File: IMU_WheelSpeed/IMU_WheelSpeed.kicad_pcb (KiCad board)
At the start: 2 copper layers, 10 parts, among them J1 Conn_01x06_Socket, U1 PeripheralSOM, U2 LSM6DSL, U4 TPS71518__SC70

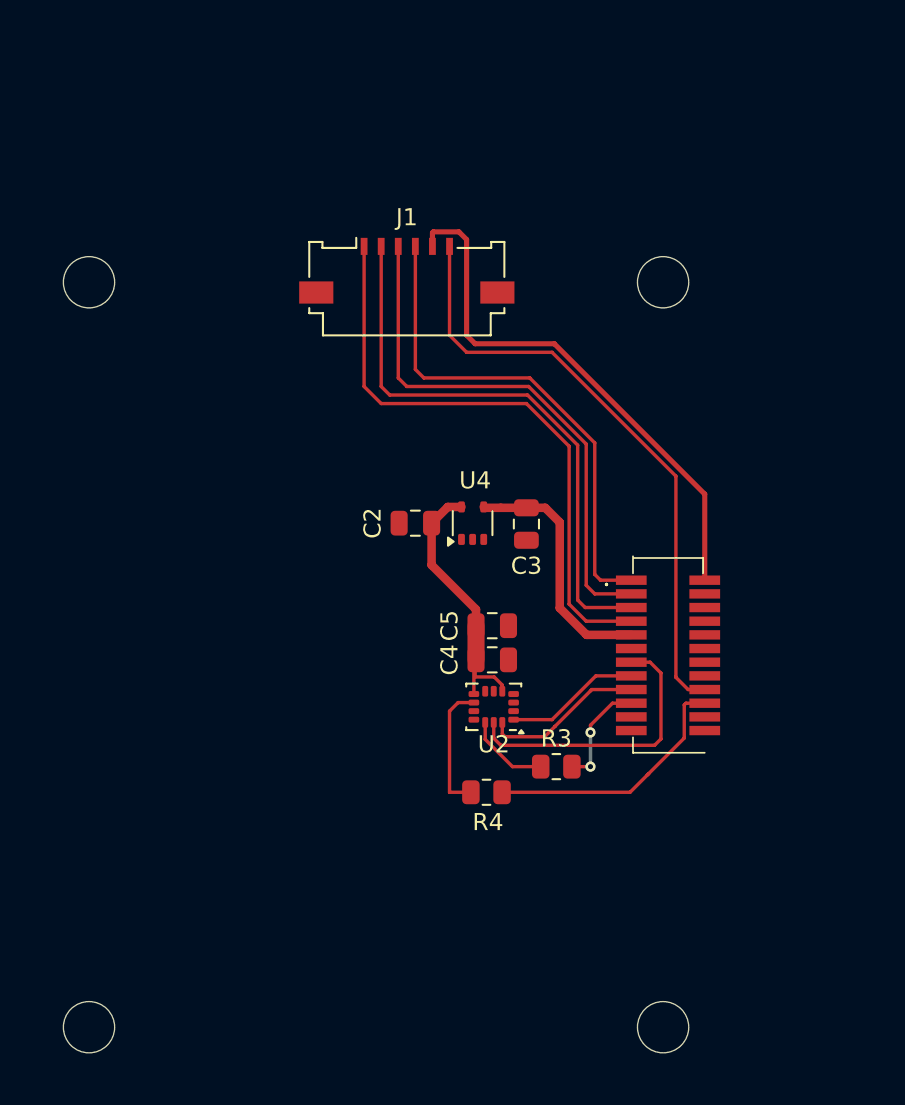
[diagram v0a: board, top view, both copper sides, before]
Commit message: added to schematic
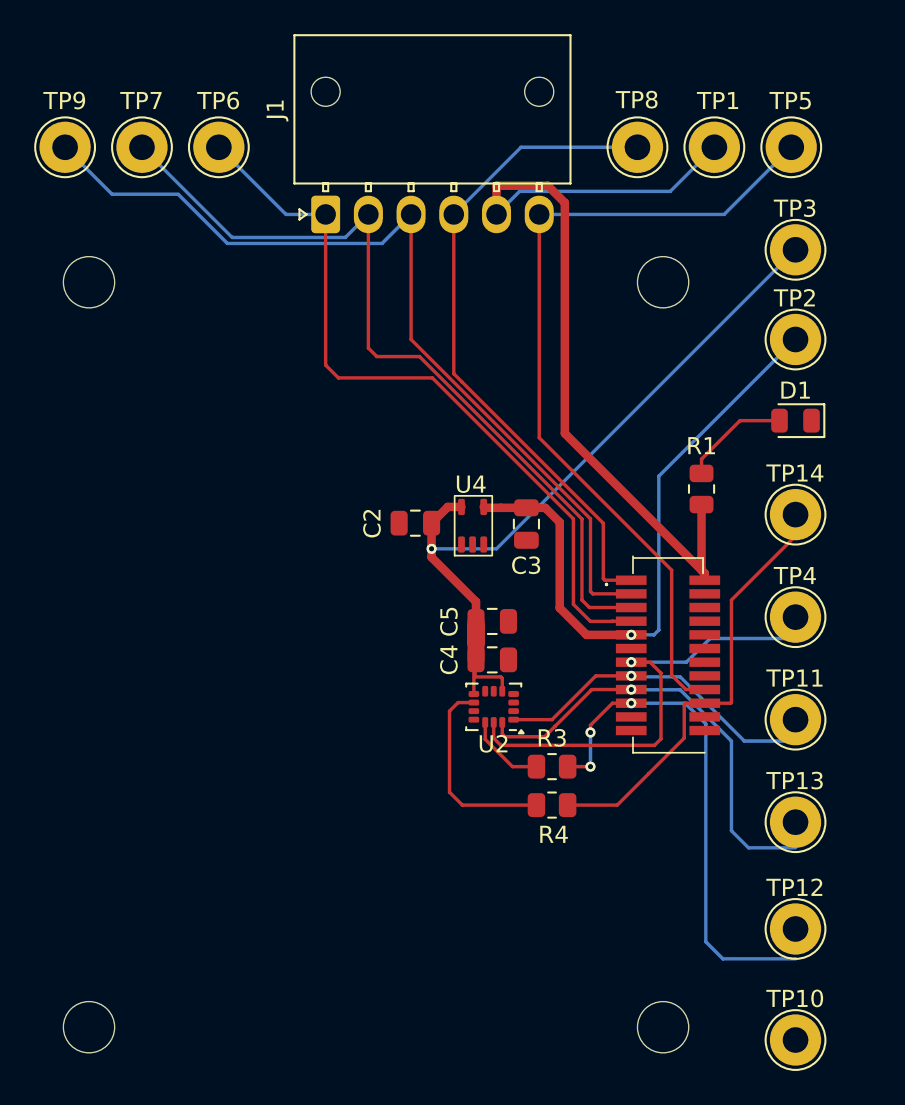
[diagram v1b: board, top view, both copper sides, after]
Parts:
- added D1: LED, LED_SMD:LED_0805_2012Metric, F.Cu at (170.8, 74.0)
- added R1: 1k, Resistor_SMD:R_0805_2012Metric, F.Cu at (165.2, 78.0)
- added TP1: VDD, TestPoint:TestPoint_THTPad_D3.0mm_Drill1.5mm, F.Cu at (166.0, 58.0)
- added TP10: VDD, TestPoint:TestPoint_THTPad_D3.0mm_Drill1.5mm, F.Cu at (170.8, 110.2)
- added TP11: VDD, TestPoint:TestPoint_THTPad_D3.0mm_Drill1.5mm, F.Cu at (170.8, 91.5)
- added TP12: VDD, TestPoint:TestPoint_THTPad_D3.0mm_Drill1.5mm, F.Cu at (170.8, 103.8)
- added TP13: VDD, TestPoint:TestPoint_THTPad_D3.0mm_Drill1.5mm, F.Cu at (170.8, 97.5)
- added TP14: VDD, TestPoint:TestPoint_THTPad_D3.0mm_Drill1.5mm, F.Cu at (170.8, 79.5)
- added TP2: VDD, TestPoint:TestPoint_THTPad_D3.0mm_Drill1.5mm, F.Cu at (170.8, 69.2)
- added TP3: VDD, TestPoint:TestPoint_THTPad_D3.0mm_Drill1.5mm, F.Cu at (170.8, 64.0)
- added TP4: VDD, TestPoint:TestPoint_THTPad_D3.0mm_Drill1.5mm, F.Cu at (170.8, 85.5)
- added TP5: VDD, TestPoint:TestPoint_THTPad_D3.0mm_Drill1.5mm, F.Cu at (170.5, 58.0)
- added TP6: VDD, TestPoint:TestPoint_THTPad_D3.0mm_Drill1.5mm, F.Cu at (137.0, 58.0)
- added TP7: VDD, TestPoint:TestPoint_THTPad_D3.0mm_Drill1.5mm, F.Cu at (132.5, 58.0)
- added TP8: VDD, TestPoint:TestPoint_THTPad_D3.0mm_Drill1.5mm, F.Cu at (161.5, 58.0)
- added TP9: VDD, TestPoint:TestPoint_THTPad_D3.0mm_Drill1.5mm, F.Cu at (128.0, 58.0)
- J1: footprint Connector_FFC-FPC:Molex_200528-0060_1x06-1MP_P1.00mm_Horizontal -> Connector_Molex:Molex_Nano-Fit_105313-xx06_1x06_P2.50mm_Horizontal
- U4: footprint Package_TO_SOT_SMD:SOT-353_SC-70-5 -> UTSVT_Special:LDO_3.3_to_1.8_2.2mmx1.3mm
- moved J1 5.50 mm to (143.2, 61.9), turned to 90 degrees
- moved U4 4.95 mm to (146.9, 80.0)
- moved R4 3.91 mm to (156.5, 96.5)
- moved C5 0.25 mm to (153.0, 85.8)
- moved R3 0.25 mm to (156.5, 94.2)
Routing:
- net <NO NET>: track 16.4 -> 46.5 mm, vias 0 -> 1
- net /IMU_CS: track 6.43 -> 30.0 mm, vias 2 -> 3
- net /LDO_3.3V: track 14.7 -> 36.7 mm, vias 0 -> 1
- net /MAGSLV_Output: track 31.7 -> 52.1 mm
- net /VDD: track 31.4 -> 50.1 mm
- net /IMUSLV_Input: track 9.44 -> 26.0 mm, vias 0 -> 1
- net /MAG_CLK: track 33.8 -> 48.3 mm
- net /Mag_High: track 35.9 -> 48.8 mm
- net /IMUSLV_Output: track 7.95 -> 19.1 mm, vias 0 -> 1
- net /IMU_CLK: track 16.9 -> 27.1 mm, vias 0 -> 1
- net /MAGSLV_Input: track 29.8 -> 39.0 mm
- net /INT2: track 15.3 -> 24.5 mm
- net /MAG_CS: track 35.2 -> 43.7 mm
- net Net-(D1-A): track 0.00 -> 6.33 mm
- net Net-(U2-INT2): track 7.63 -> 11.8 mm

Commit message: redid layout
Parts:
- removed R4: 10k, Resistor_SMD:R_0805_2012Metric
- removed TP12, TP13, TP2, TP4: VDD, TestPoint:TestPoint_THTPad_D3.0mm_Drill1.5mm
- added J3: Conn_01x03_Socket, Connector_Molex:Molex_Nano-Fit_105313-xx03_1x03_P2.50mm_Horizontal, F.Cu at (169.4, 102.8)
- added R2: 10k, Resistor_SMD:R_0805_2012Metric, F.Cu at (153.0, 95.0)
- TP10: value VDD -> IMU_I2C_SDA
- TP11: value VDD -> IMU_CLK
- TP14: value VDD -> GND
- TP5: value VDD -> Mag_High
- TP6: value VDD -> MAG_CS
- TP7: value VDD -> MAG_CLK
- TP8: value VDD -> MAGSLV_I
- TP9: value VDD -> MAGSLV_O
- U4: footprint UTSVT_Special:LDO_3.3_to_1.8_2.2mmx1.3mm -> UTSVT_Power:LDO_3.3_to_1.8_2.2mmx1.3mm
- moved TP10 19.1 mm to (173.0, 91.2)
- moved TP11 6.41 mm to (173.0, 85.5)
- moved R3 4.58 mm to (153.0, 97.2)
- moved D1 2.30 mm to (170.2, 71.8)
- moved TP3 2.30 mm to (173.0, 64.5)
- moved TP14 2.26 mm to (173.0, 79.8)
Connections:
- net Net-(D1-A) renamed /LTE_D1
- C3 pad 1: /LDO_3.3V -> /VDD_3.3V
- J1 pad 5: /VDD -> /VDD_3.3V
- R1 pad 2: /VDD -> /VDD_3.3V
- R3 pad 1: Net-(U2-CS) -> <NO NET>
- R3 pad 2: /IMU_CS -> /IMU_I2C_SDA
- TP10 pad 1: /IMU_CS -> /IMU_I2C_SDA
- TP11 pad 1: /IMU_CLK -> /IMU_I2C_SLC
- U1 pad 13: /IMU_CLK -> unconnected-(U1-SPI1_SCK-Pad13)
- U1 pad 14: unconnected-(U1-I2C1_SCL-Pad14) -> /IMU_I2C_SCL
- U1 pad 15: /IMUSLV_Output -> unconnected-(U1-SPI1_MISO-Pad15)
- U1 pad 16: unconnected-(U1-I2C1_SDA-Pad16) -> /IMU_I2C_SDA
- U1 pad 17: /IMUSLV_Input -> unconnected-(U1-SPI1_MOSI-Pad17)
- U1 pad 19: /IMU_CS -> unconnected-(U1-SPI1_NSS-Pad19)
- U1 pad 2: /VDD -> /VDD_3.3V
- U1 pad 20: /INT2 -> /GPIO_1
- U1 pad 9: /LDO_3.3V -> /VDD_3.3V
- U2 pad 1: /IMUSLV_Output -> unconnected-(U2-SDO/SA0-Pad1)
- U2 pad 12: Net-(U2-CS) -> unconnected-(U2-CS-Pad12)
- U2 pad 13: /IMU_CLK -> /IMU_I2C_SCL
- U2 pad 14: /IMUSLV_Input -> /IMU_I2C_SDA
- U2 pad 9: Net-(U2-INT2) -> unconnected-(U2-INT2-Pad9)
- U4 pad 4: /LDO_3.3V -> /VDD_3.3V
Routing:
- net /VDD_3.3V: track 0.00 -> 70.2 mm, vias 0 -> 2
- net /LDO_3.3V: track 36.7 -> 0.00 mm, vias 1 -> 0
- net /VDD: track 50.1 -> 14.4 mm
- net /IMU_I2C_SDA: track 0.00 -> 32.9 mm, vias 0 -> 3
- net /IMU_CS: track 30.0 -> 0.00 mm, vias 3 -> 0
- net /IMU_I2C_SCL: track 0.00 -> 29.1 mm, vias 0 -> 1
- net /IMU_CLK: track 27.1 -> 0.00 mm, vias 1 -> 0
- net /IMUSLV_Input: track 26.0 -> 0.00 mm, vias 1 -> 0
- net /INT2: track 24.5 -> 0.00 mm
- net <NO NET>: track 46.5 -> 68.0 mm
- net /IMUSLV_Output: track 19.1 -> 0.00 mm, vias 1 -> 0
- net /GPIO_1: track 0.00 -> 13.4 mm
- net Net-(U2-INT2): track 11.8 -> 0.00 mm
- net Net-(U2-CS): track 4.65 -> 0.00 mm
- net /LTE_D1: track 6.33 -> 8.37 mm
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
